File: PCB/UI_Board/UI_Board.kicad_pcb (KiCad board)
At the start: 2 copper layers, 169.8 x 35 mm, 18 parts, among them J1 DISPLAY, J2 CABLE, SW1 SW_UP, SW2 SW_DWN, SW3 SW_PRE_1, SW4 SW_PRE_2

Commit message: Updated PCB files
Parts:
- removed H1, H2: MountingHole, MountingHole:MountingHole_3.2mm_M3
- added C1: 0.1uF, Capacitor_THT:C_Rect_L7.2mm_W3.5mm_P5.00mm_FKS2_FKP2_MKS2_MKP2, F.Cu at (41.5, 107.5)
- moved H3 100.2 mm to (107.2, 98.3)
- moved H8 97.4 mm to (44.0, 123.5)
- moved SW1 92.5 mm to (120.0, 101.5)
- moved H4 89.2 mm to (107.2, 126.3)
- moved SW4 86.5 mm to (140.5, 118.5)
- moved R1 86.3 mm to (120.0, 111.0), turned to 0 degrees
- moved H5 84.7 mm to (162.5, 123.5)
- moved SW2 84.4 mm to (120.0, 118.5)
- moved J2 76.3 mm to (86.0, 103.2), turned to -90 degrees
- moved J1 73.4 mm to (50.0, 104.5)
- moved ? 70.5 mm to (161.1, 110.4)
- moved R2 69.6 mm to (147.0, 111.0), turned to 180 degrees
- moved R3 62.6 mm to (147.0, 114.5)
- moved H7 59.9 mm to (44.0, 101.5)
- moved SW3 57.5 mm to (140.5, 101.5)
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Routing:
- net /BTNS: track 167.5 -> 74.5 mm
- net Net-(R3-Pad1): track 25.3 -> 10.5 mm
- net /CS: track 39.9 -> 48.8 mm
- net /SCL: track 30.7 -> 37.5 mm
- net Net-(R2-Pad1): track 11.9 -> 18.1 mm
- net /DC: track 41.7 -> 36.4 mm
- net /RST: track 39.8 -> 36.5 mm
- net /SDA: track 34.2 -> 36.6 mm
- net Net-(R1-Pad1): track 15.9 -> 14.0 mm
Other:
- board size 169.8 x 35 mm -> 133 x 40.2 mm
- board text added: "DISPLAY"
- board text added: "MoTrotten UI Board v0.0.2 June-26 Carmel Barak"

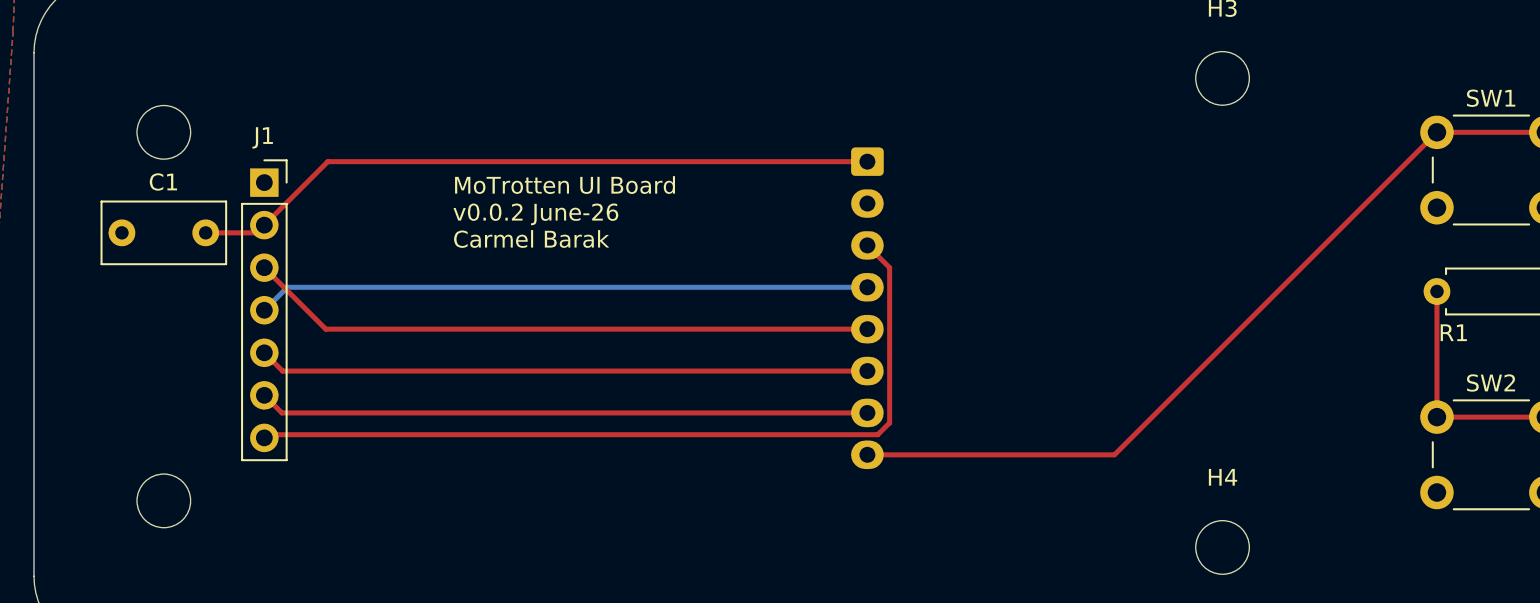
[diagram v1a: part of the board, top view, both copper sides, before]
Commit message: Fixed display socket orientation and rotated cable JST socket to match
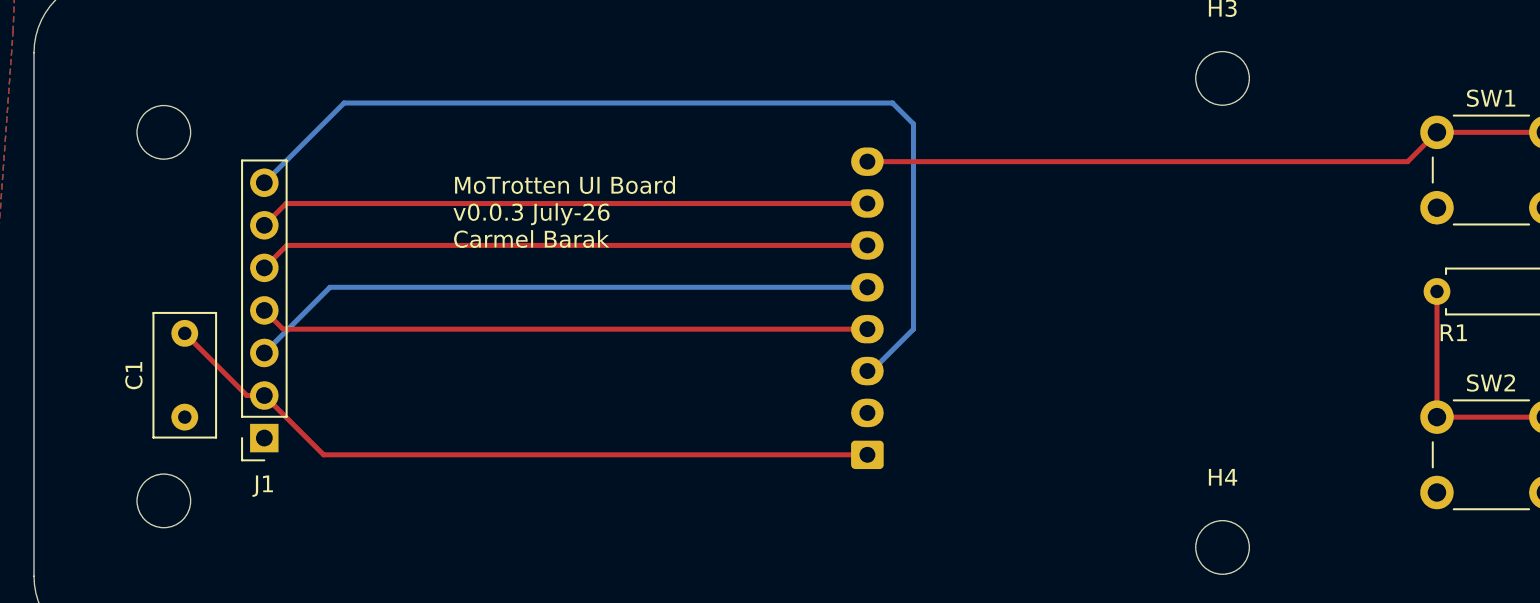
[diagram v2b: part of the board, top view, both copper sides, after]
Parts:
- moved J2 17.5 mm to (86.0, 120.8), turned to 90 degrees
- moved J1 15.2 mm to (50.0, 119.8), turned to 180 degrees
- moved C1 11.6 mm to (45.2, 118.5), turned to 90 degrees
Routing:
- net /CS: track 48.8 -> 57.3 mm
- net /BTNS: track 74.5 -> 67.2 mm
- net /3V3: track 41.3 -> 43.8 mm
- net /DC: track 36.4 -> 37.2 mm
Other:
- board text added: "MoTrotten UI Board v0.0.3 July-26 Carmel Barak"
- board text removed: "MoTrotten UI Board v0.0.2 June-26 Carmel Barak"
